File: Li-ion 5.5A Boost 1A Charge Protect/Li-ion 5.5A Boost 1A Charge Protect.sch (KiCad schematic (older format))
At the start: 55 parts, among them J1 USB_C_FEMALE, Q1 BUK6D30-40E, SW1 SW_DPST, U1 AP9101CK6, U2 ECH8695R-TL-W, U3 MCP73833T, U4 PAM2423AECADJR

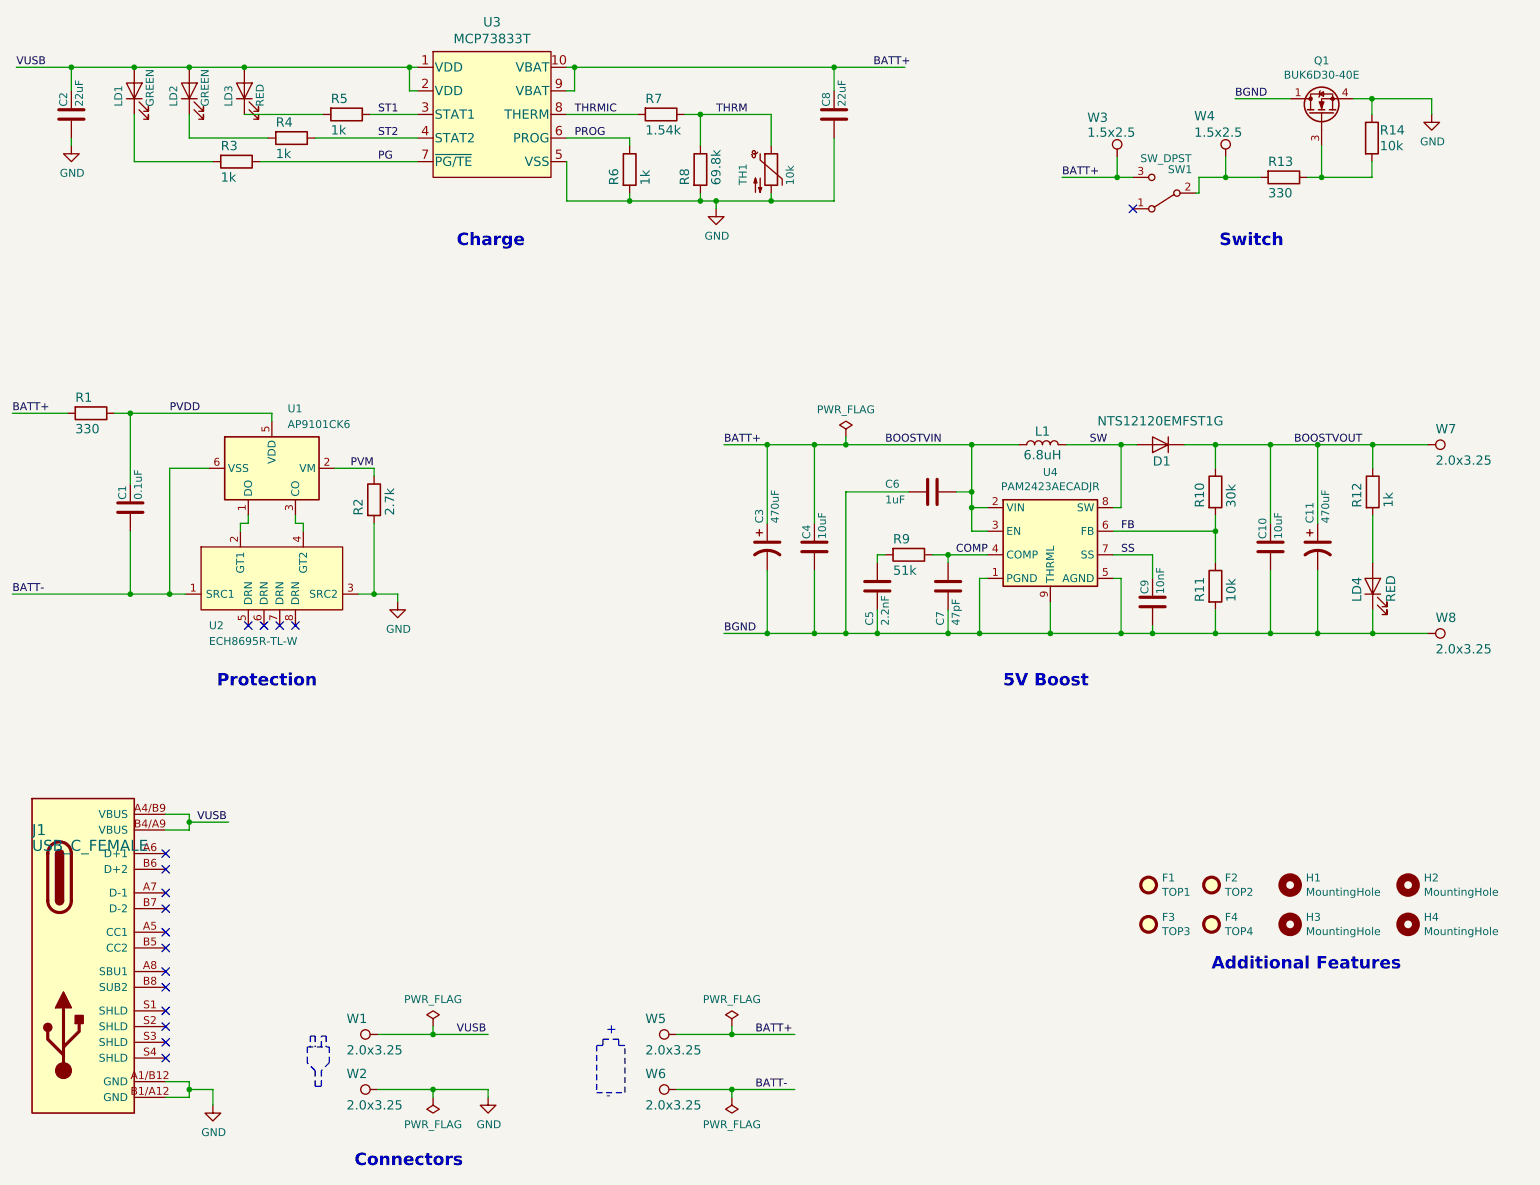
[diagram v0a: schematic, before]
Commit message: Renaming 5A to 5.5A
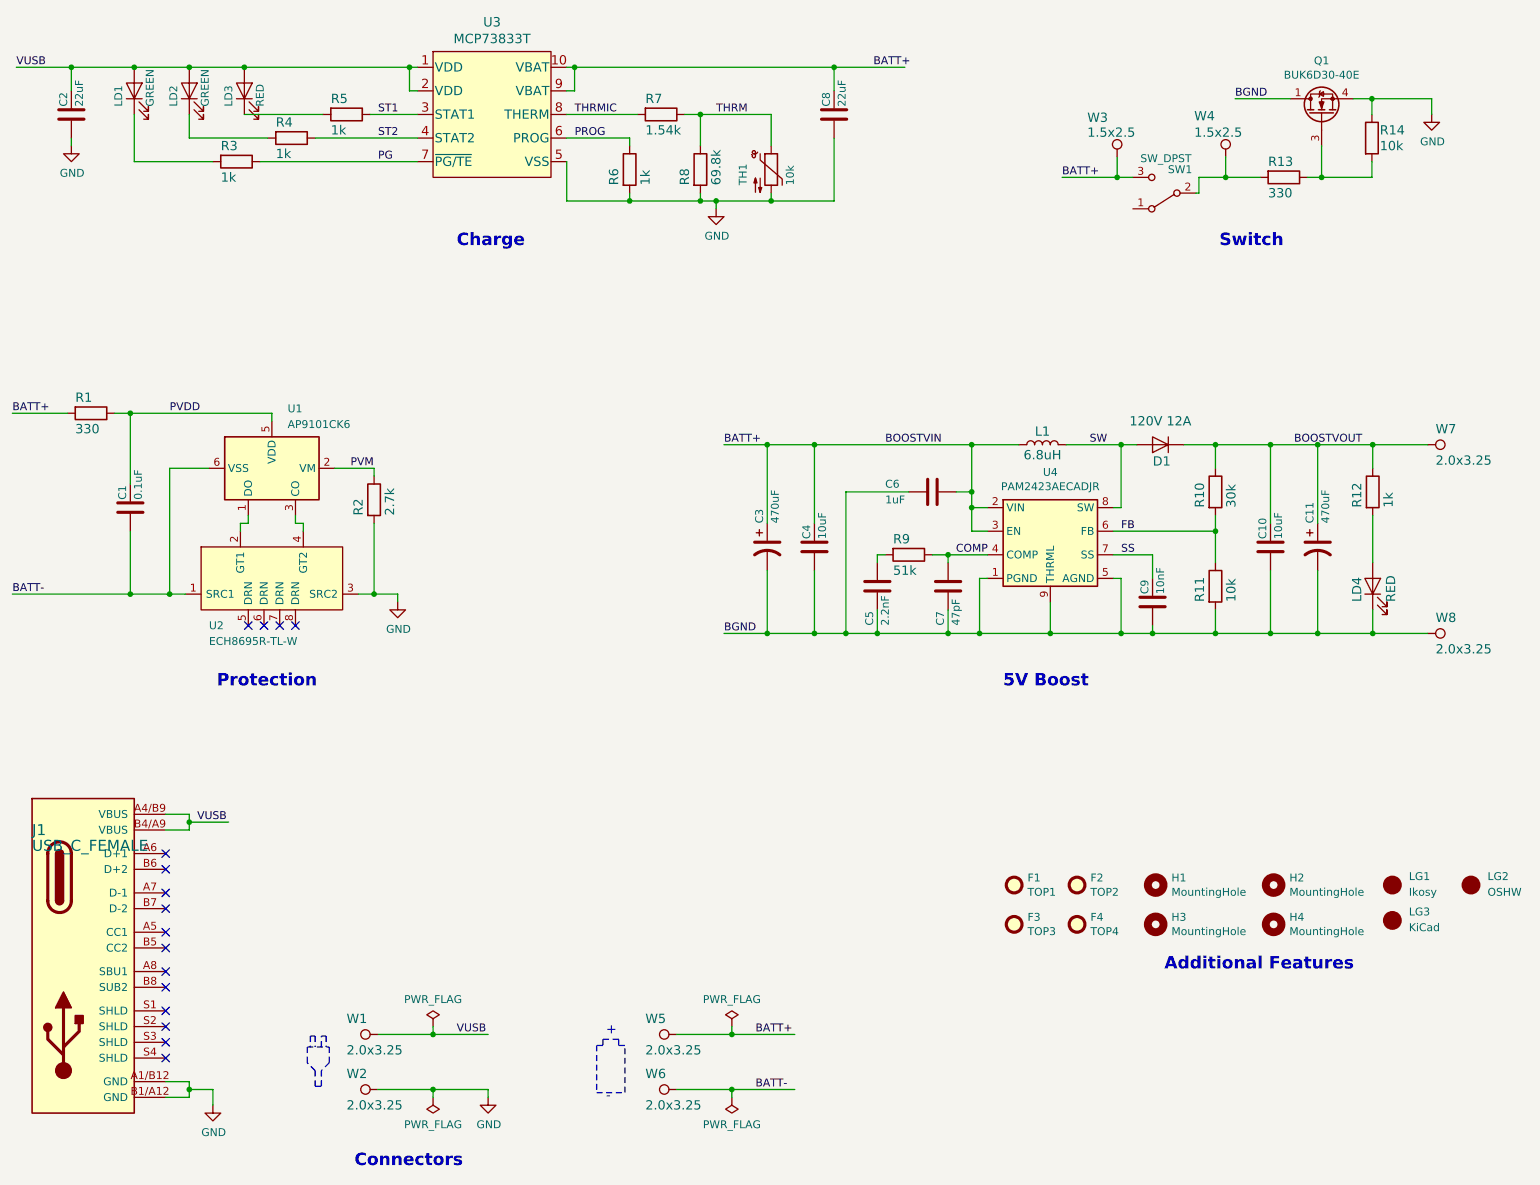
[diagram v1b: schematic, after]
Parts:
- added LG1: Logo, Logo_LE:Ikosy-Logo_Type1_10.3x2mm_SilkScreen, symbol Frequently_Used_LE:Logo
- added LG2: Logo, Logo_LE:OSHW-Symbol_3mm_Silkscreen, symbol Frequently_Used_LE:Logo
- added LG3: Logo, Logo_LE:KiCad-Logo3_3mm_SilkScreen, symbol Frequently_Used_LE:Logo
- D1: value NTS12120EMFST1G -> 120V 12A
- H1, H2, H3, H4: Source (none) -> None; Source 2 (none) -> Mouser
- Q1: Description (none) -> N-Channel 6A (Ta), 18A (Tc) 2W (Ta), 19W (Tc) Surface Mount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; Manufacturer Name (none) -> Nexperia; Manufacturer Part No. (none) -> BUK6D30-40EX; Source (none) -> None; Source 2 (none) -> Mouser; Source 2 Part No. (none) -> 771-BUK6D30-40EX; Source Part No. (none) -> 1727-BUK6D30-40EXCT-ND
- R1, R13: Manufacturer Part No. ESR03EZPF3300 -> BUK6D30-40EX
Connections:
- wire segments 174 -> 172
- no-connect marks 17 -> 16
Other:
- moved on the sheet: F1, F2, F3, F4, H1, H2, H3, H4

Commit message: Component extraction
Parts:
- removed C1: 0.1uF, Frequently_Used_LE:0603_1608Metric, symbol Frequently_Used_LE:C
- removed C10, C4: 10uF, Frequently_Used_LE:0603_1608Metric, symbol Frequently_Used_LE:C
- removed C11, C3: 470uF, Li_Ion_LE:CP_Elec_10x10.5, symbol Frequently_Used_LE:CP1
- removed C2, C8: 22uF, Frequently_Used_LE:0603_1608Metric, symbol Frequently_Used_LE:C
- removed C5: 2.2nF, Frequently_Used_LE:0603_1608Metric, symbol Frequently_Used_LE:C
- removed C6: 1uF, Frequently_Used_LE:0603_1608Metric, symbol Frequently_Used_LE:C
- removed C7: 47pF, Frequently_Used_LE:0603_1608Metric, symbol Frequently_Used_LE:C
- removed C9: 10nF, Frequently_Used_LE:0603_1608Metric, symbol Frequently_Used_LE:C
- removed D1: 120V 12A, Li_Ion_LE:NTS12120EMFST1G, symbol Li_Ion_LE:D_NTS12120EMFST1G
- removed L1: 6.8uH, Li_Ion_LE:L_MGV1004, symbol Frequently_Used_LE:L
- removed LD1, LD2: GREEN, Frequently_Used_LE:LED_0805_2012Metric, symbol Frequently_Used_LE:LED
- removed LD3, LD4: RED, Frequently_Used_LE:LED_0805_2012Metric, symbol Frequently_Used_LE:LED
- removed Q1: BUK6D30-40E, Li_Ion_LE:BUK6D3040EX, symbol Li_Ion_LE:BUK6D30-40E
- removed R1, R13: 330, Frequently_Used_LE:0603_1608Metric, symbol Frequently_Used_LE:R
- removed R10: 30k, Frequently_Used_LE:0603_1608Metric, symbol Frequently_Used_LE:R
- removed R11, R14: 10k, Frequently_Used_LE:0603_1608Metric, symbol Frequently_Used_LE:R
- removed R12, R3, R4, R5, R6: 1k, Frequently_Used_LE:0603_1608Metric, symbol Frequently_Used_LE:R
- removed R2: 2.7k, Frequently_Used_LE:0603_1608Metric, symbol Frequently_Used_LE:R
- removed R7: 1.54k, Frequently_Used_LE:0603_1608Metric, symbol Frequently_Used_LE:R
- removed R8: 69.8k, Frequently_Used_LE:0603_1608Metric, symbol Frequently_Used_LE:R
- removed R9: 51k, Frequently_Used_LE:0603_1608Metric, symbol Frequently_Used_LE:R
- removed SW1: SW_DPST, Button_Switch_LE:CL-SB-22A_Edge, symbol Button_Switch_LE:CL-SB-22A
- removed TH1: 10k, Frequently_Used_LE:0603_1608Metric, symbol Li_Ion_LE:Thermistor_NTC
- removed U1: AP9101CK6, Li_Ion_LE:SOT-23-6, symbol Li_Ion_LE:AP9101CK6
- removed U2: ECH8695R-TL-W, Li_Ion_LE:SOT65P280X95-8N, symbol Li_Ion_LE:ECH8695R-TL-W_Gates_on_Top
- removed U3: MCP73833T, Li_Ion_LE:MCP73833, symbol Li_Ion_LE:MCP73833T
- removed U4: PAM2423AECADJR, Li_Ion_LE:PAM2423AECADJR, symbol Li_Ion_LE:PAM2423AECADJR
- F1, F2, F3, F4, H1, H2, H3, H4, LG1, LG2, LG3, W1, W2, W3, W4, W5, W6, W7, W8: Source None -> (none); Source 1 (none) -> None; Source 1 Part No. (none) -> None; Source Part No. None -> (none)
- J1: Source Digikey -> (none); Source 1 (none) -> Digikey; Source 1 Part No. (none) -> 2073-USB4110-GF-A-1-ND; Source Part No. 2073-USB4110-GF-A-1-ND -> (none)
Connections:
- net labels removed: BOOSTVIN, BOOSTVOUT, COMP, FB, PG, PROG, PVDD, PVM, SS, ST1, ST2, SW, THRM, THRMIC
- wire segments 172 -> 44
- no-connect marks 16 -> 12
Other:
- note added: "Boost"
- note removed: "5V Boost"
- moved on the sheet: F1, F2, F3, F4, H1, H2, H3, H4, J1, LG1, LG2, LG3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
